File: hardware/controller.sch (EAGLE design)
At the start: 44 parts, among them J1 AVR_SPI_PRG_6NS, J10 22-27-2041-04, J11 22-27-2041-04, J2 ATX24RH, J3 22-27-2041-04, J4 22-27-2041-04, J5 22-27-2021-02, J6 22-27-2021-02, J7 22-27-2031-03, J8 22-27-2041-04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

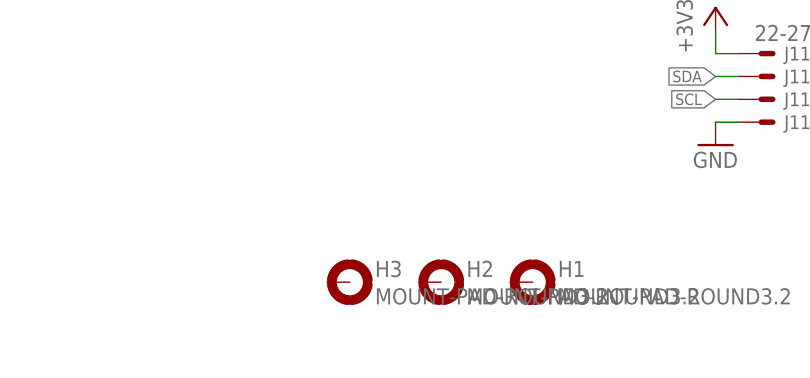
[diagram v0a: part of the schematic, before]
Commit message: Hardware: Add fourth hole and different crystal footprint.
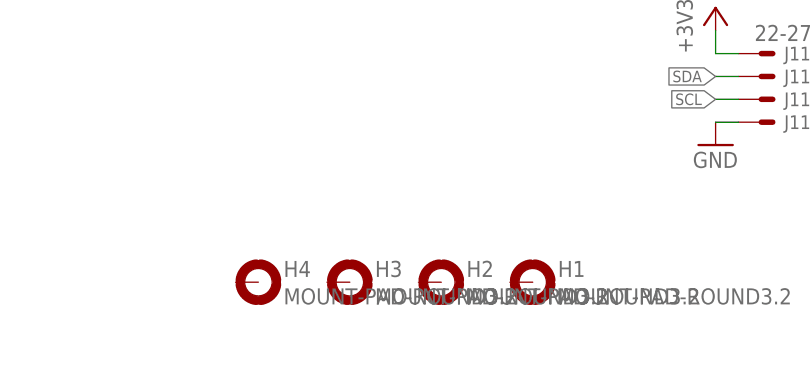
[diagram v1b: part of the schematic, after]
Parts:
- added H4: MOUNT-PAD-ROUND3.2, holes:MOUNT-PAD-ROUND3.2
- Y1: device SparkFun-FreqCtrl:CRYSTALSMD -> SparkFun-FreqCtrl:CRYSTALHC49UV
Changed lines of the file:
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@@
 <part name="P+1" library="supply1" deviceset="+5V" device=""/>
 <part name="J1" library="SparkFun-Connectors" deviceset="AVR_SPI_PRG_6" device="NS"/>
-<part name="Y1" library="SparkFun-FreqCtrl" deviceset="CRYSTAL" device="SMD"/>
+<part name="Y1" library="SparkFun-FreqCtrl" deviceset="CRYSTAL" device="HC49UV"/>
 <part name="P+2" library="supply1" deviceset="+5V" device=""/>
 <part name="GND2" library="supply1" deviceset="GND" device=""/>
@@
 <part name="R13" library="rcl" deviceset="R-EU_" device="R0603" value="1k"/>
 <part name="P+13" library="supply1" deviceset="+5V" device=""/>
+<part name="H4" library="holes" deviceset="MOUNT-PAD-ROUND" device="3.2"/>
 </parts>
 <sheets>
@@
 <instance part="R13" gate="G$1" x="20.32" y="81.28"/>
 <instance part="P+13" gate="1" x="12.7" y="86.36"/>
+<instance part="H4" gate="G$1" x="119.38" y="15.24"/>
 </instances>
 <busses>

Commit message: Hardware: Redesign layout of controller PCB.
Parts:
- removed R4: 1k, rcl:R-EU_R0603
- added C1, C2, C5, C6: (no value), rcl:C-EUC0603
- R1: value (none) -> 30
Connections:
- removed net N$8: R4.2, U$1.ALERT
- net +3V3: now also C5.1, C6.1, R13.1; no longer R4.1
- net +5V: now also C1.1, C2.1; no longer R13.1
- net GND: now also C1.2, C2.2, C5.2, C6.2
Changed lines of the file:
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@@
 <part name="+3V4" library="supply1" deviceset="+3V3" device=""/>
 <part name="+3V5" library="supply1" deviceset="+3V3" device=""/>
-<part name="R1" library="rcl" deviceset="R-EU_" device="R0603"/>
+<part name="R1" library="rcl" deviceset="R-EU_" device="R0603" value="30"/>
 <part name="R2" library="rcl" deviceset="R-EU_" device="R0603" value="56k"/>
 <part name="R3" library="rcl" deviceset="R-EU_" device="R0603" value="56k"/>
@@
 <part name="+3V6" library="supply1" deviceset="+3V3" device=""/>
 <part name="GND9" library="supply1" deviceset="GND" device=""/>
-<part name="R4" library="rcl" deviceset="R-EU_" device="R0603" value="1k"/>
 <part name="+3V8" library="supply1" deviceset="+3V3" device=""/>
 <part name="J2" library="hauser" deviceset="ATX24" device="RH"/>
@@
 <part name="H3" library="holes" deviceset="MOUNT-PAD-ROUND" device="3.2"/>
 <part name="R13" library="rcl" deviceset="R-EU_" device="R0603" value="1k"/>
-<part name="P+13" library="supply1" deviceset="+5V" device=""/>
 <part name="H4" library="holes" deviceset="MOUNT-PAD-ROUND" device="3.2"/>
+<part name="C1" library="rcl" deviceset="C-EU" device="C0603"/>
+<part name="C2" library="rcl" deviceset="C-EU" device="C0603"/>
+<part name="C5" library="rcl" deviceset="C-EU" device="C0603"/>
+<part name="C6" library="rcl" deviceset="C-EU" device="C0603"/>
+<part name="+3V10" library="supply1" deviceset="+3V3" device=""/>
+<part name="GND12" library="supply1" deviceset="GND" device=""/>
+<part name="P+14" library="supply1" deviceset="+5V" device=""/>
+<part name="+3V11" library="supply1" deviceset="+3V3" device=""/>
 </parts>
 <sheets>
@@
 <instance part="+3V6" gate="G$1" x="40.64" y="114.3"/>
 <instance part="GND9" gate="1" x="40.64" y="83.82"/>
-<instance part="R4" gate="G$1" x="63.5" y="99.06" rot="R270"/>
 <instance part="+3V8" gate="G$1" x="58.42" y="109.22"/>
 <instance part="J2" gate="G$1" x="228.6" y="147.32"/>
@@
 <instance part="H3" gate="G$1" x="129.54" y="15.24"/>
 <instance part="R13" gate="G$1" x="20.32" y="81.28"/>
-<instance part="P+13" gate="1" x="12.7" y="86.36"/>
 <instance part="H4" gate="G$1" x="119.38" y="15.24"/>
+<instance part="C1" gate="G$1" x="167.64" y="86.36"/>
+<instance part="C2" gate="G$1" x="175.26" y="86.36"/>
+<instance part="C5" gate="G$1" x="182.88" y="86.36"/>
+<instance part="C6" gate="G$1" x="190.5" y="86.36"/>
+<instance part="+3V10" gate="G$1" x="190.5" y="99.06"/>
+<instance part="GND12" gate="1" x="175.26" y="73.66"/>
+<instance part="P+14" gate="1" x="175.26" y="99.06"/>
+<instance part="+3V11" gate="G$1" x="12.7" y="86.36"/>
 </instances>
 <busses>
@@
 </segment>
 <segment>
-<pinref part="R13" gate="G$1" pin="1"/>
-<pinref part="P+13" gate="1" pin="+5V"/>
-<wire x1="15.24" y1="81.28" x2="12.7" y2="81.28" width="0.1524" layer="91"/>
-<wire x1="12.7" y1="81.28" x2="12.7" y2="83.82" width="0.1524" layer="91"/>
+<pinref part="C2" gate="G$1" pin="1"/>
+<pinref part="P+14" gate="1" pin="+5V"/>
+<wire x1="175.26" y1="88.9" x2="175.26" y2="91.44" width="0.1524" layer="91"/>
+<pinref part="C1" gate="G$1" pin="1"/>
+<wire x1="175.26" y1="91.44" x2="175.26" y2="96.52" width="0.1524" layer="91"/>
+<wire x1="167.64" y1="88.9" x2="167.64" y2="91.44" width="0.1524" layer="91"/>
+<wire x1="167.64" y1="91.44" x2="175.26" y2="91.44" width="0.1524" layer="91"/>
+<junction x="175.26" y="91.44"/>
 </segment>
 </net>
@@
 <junction x="111.76" y="116.84"/>
 </segment>
+<segment>
+<pinref part="C1" gate="G$1" pin="2"/>
+<wire x1="167.64" y1="81.28" x2="167.64" y2="78.74" width="0.1524" layer="91"/>
+<wire x1="167.64" y1="78.74" x2="175.26" y2="78.74" width="0.1524" layer="91"/>
+<pinref part="C2" gate="G$1" pin="2"/>
+<wire x1="175.26" y1="78.74" x2="175.26" y2="81.28" width="0.1524" layer="91"/>
+<pinref part="GND12" gate="1" pin="GND"/>
+<wire x1="175.26" y1="76.2" x2="175.26" y2="78.74" width="0.1524" layer="91"/>
+<junction x="175.26" y="78.74"/>
+<pinref part="C6" gate="G$1" pin="2"/>
+<wire x1="190.5" y1="81.28" x2="190.5" y2="78.74" width="0.1524" layer="91"/>
+<wire x1="190.5" y1="78.74" x2="182.88" y2="78.74" width="0.1524" layer="91"/>
+<pinref part="C5" gate="G$1" pin="2"/>
+<wire x1="182.88" y1="78.74" x2="175.26" y2="78.74" width="0.1524" layer="91"/>
+<wire x1="182.88" y1="81.28" x2="182.88" y2="78.74" width="0.1524" layer="91"/>
+<junction x="182.88" y="78.74"/>
+</segment>
 </net>
 <net name="N$1" class="0">
@@
 <wire x1="55.88" y1="99.06" x2="58.42" y2="99.06" width="0.1524" layer="91"/>
 <pinref part="+3V8" gate="G$1" pin="+3V3"/>
-<pinref part="R4" gate="G$1" pin="1"/>
-<wire x1="63.5" y1="104.14" x2="58.42" y2="104.14" width="0.1524" layer="91"/>
 </segment>
 <segment>
@@
 <junction x="243.84" y="165.1"/>
 </segment>
+<segment>
+<pinref part="C6" gate="G$1" pin="1"/>
+<pinref part="+3V10" gate="G$1" pin="+3V3"/>
+<wire x1="190.5" y1="88.9" x2="190.5" y2="91.44" width="0.1524" layer="91"/>
+<pinref part="C5" gate="G$1" pin="1"/>
+<wire x1="190.5" y1="91.44" x2="190.5" y2="96.52" width="0.1524" layer="91"/>
+<wire x1="182.88" y1="88.9" x2="182.88" y2="91.44" width="0.1524" layer="91"/>
+<wire x1="182.88" y1="91.44" x2="190.5" y2="91.44" width="0.1524" layer="91"/>
+<junction x="190.5" y="91.44"/>
+</segment>
+<segment>
+<pinref part="R13" gate="G$1" pin="1"/>
+<wire x1="15.24" y1="81.28" x2="12.7" y2="81.28" width="0.1524" layer="91"/>
+<wire x1="12.7" y1="81.28" x2="12.7" y2="83.82" width="0.1524" layer="91"/>
+<pinref part="+3V11" gate="G$1" pin="+3V3"/>
+</segment>
 </net>
 <net name="N$3" class="0">
@@
 </segment>
 </net>
-<net name="N$8" class="0">
-<segment>
-<pinref part="U$1" gate="G$1" pin="ALERT"/>
-<pinref part="R4" gate="G$1" pin="2"/>
-<wire x1="55.88" y1="93.98" x2="63.5" y2="93.98" width="0.1524" layer="91"/>
-</segment>
-</net>

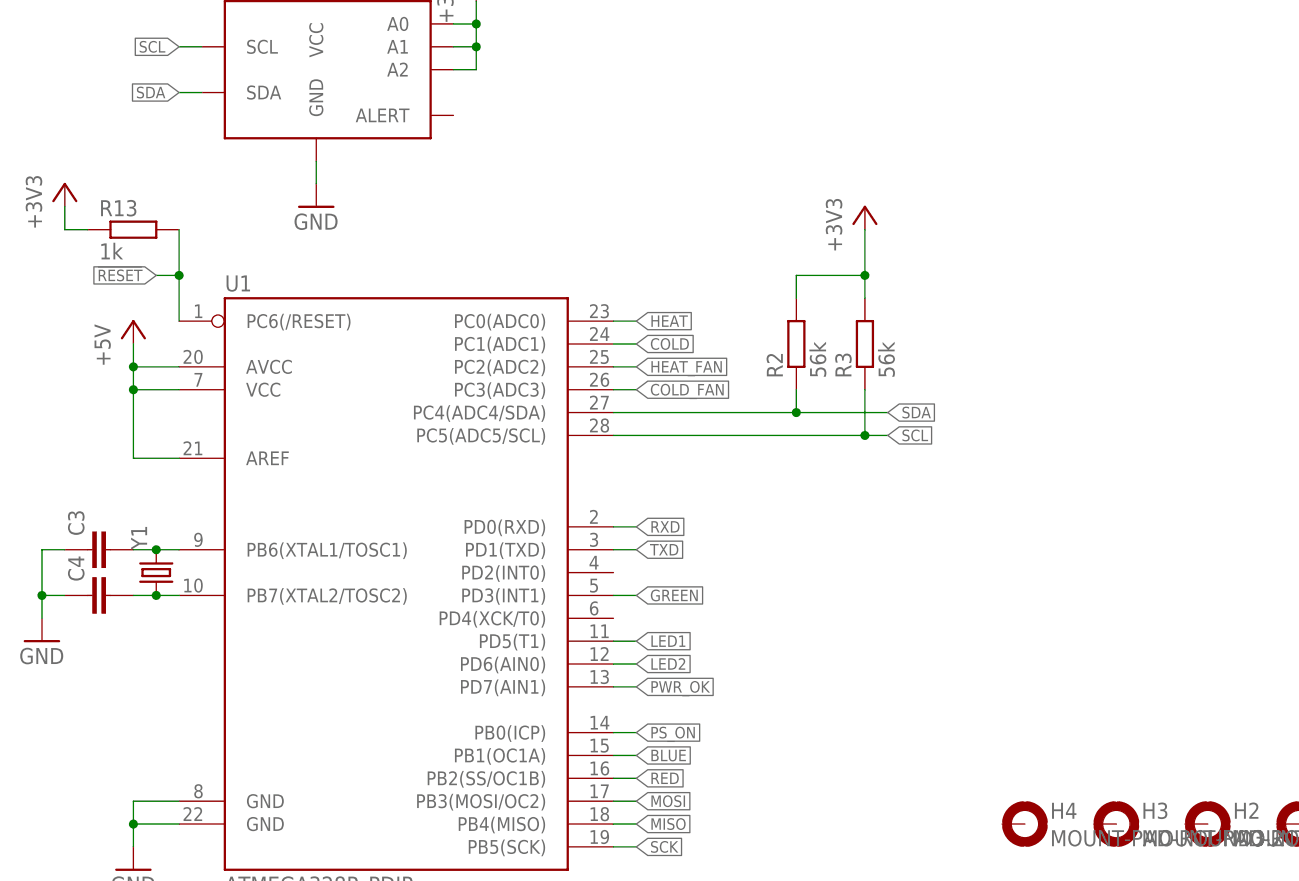
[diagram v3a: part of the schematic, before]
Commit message: Hardware: Add reset push button to PCB.
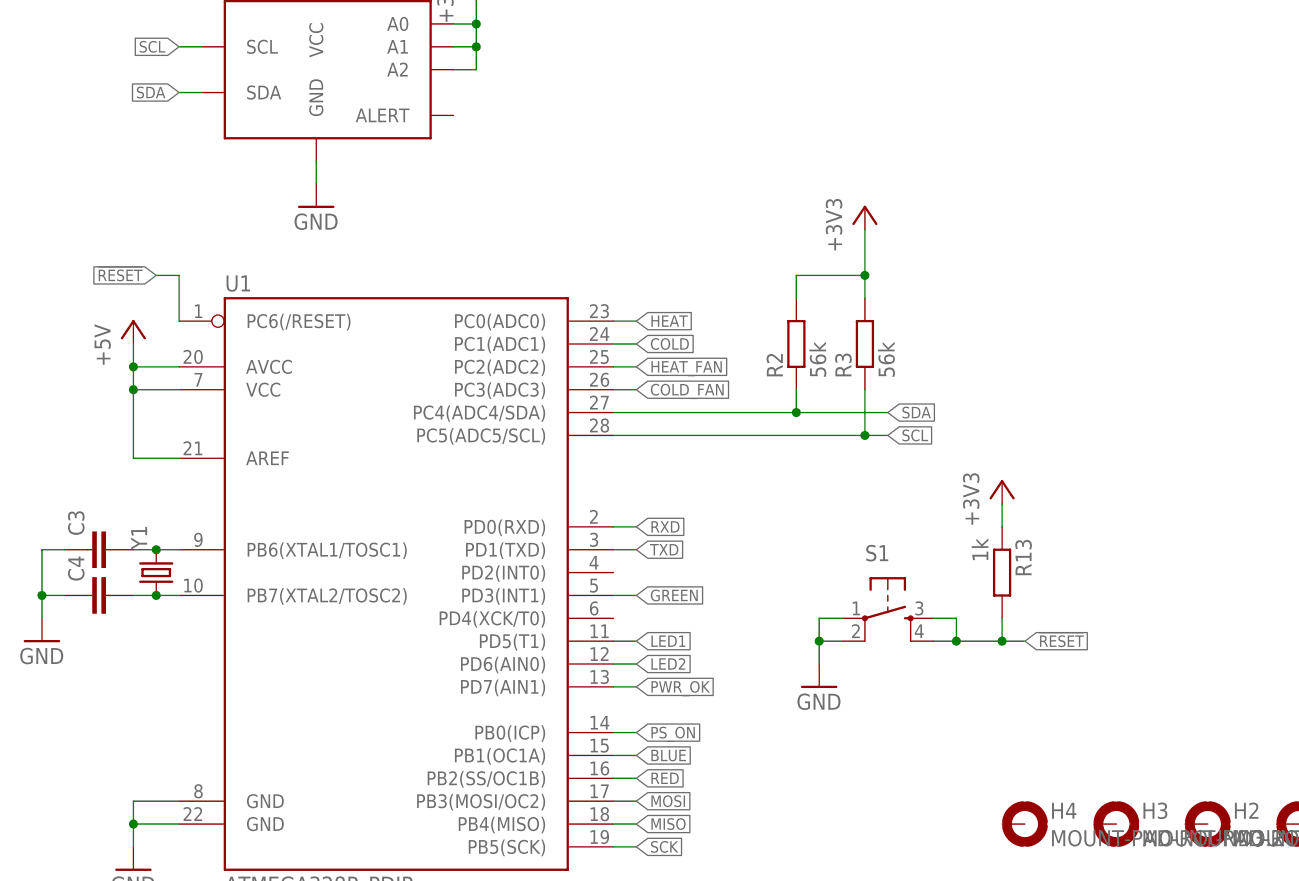
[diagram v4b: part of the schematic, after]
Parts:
- added S1: (no value), SparkFun-Electromechanical:TAC_SWITCHPTH
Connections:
- net !RESET: now also S1.3, S1.4
- net GND: now also S1.1, S1.2
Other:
- moved on the sheet: R13
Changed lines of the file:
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@@
 <part name="P+14" library="supply1" deviceset="+5V" device=""/>
 <part name="+3V11" library="supply1" deviceset="+3V3" device=""/>
+<part name="S1" library="SparkFun-Electromechanical" deviceset="TAC_SWITCH" device="PTH"/>
+<part name="GND13" library="supply1" deviceset="GND" device=""/>
 </parts>
 <sheets>
@@
 <instance part="H2" gate="G$1" x="139.7" y="15.24"/>
 <instance part="H3" gate="G$1" x="129.54" y="15.24"/>
-<instance part="R13" gate="G$1" x="20.32" y="81.28"/>
+<instance part="R13" gate="G$1" x="116.84" y="43.18" rot="R270"/>
 <instance part="H4" gate="G$1" x="119.38" y="15.24"/>
 <instance part="C1" gate="G$1" x="167.64" y="86.36"/>
@@
 <instance part="GND12" gate="1" x="175.26" y="73.66"/>
 <instance part="P+14" gate="1" x="175.26" y="99.06"/>
-<instance part="+3V11" gate="G$1" x="12.7" y="86.36"/>
+<instance part="+3V11" gate="G$1" x="116.84" y="53.34"/>
+<instance part="S1" gate="S" x="104.14" y="38.1"/>
+<instance part="GND13" gate="1" x="96.52" y="30.48"/>
 </instances>
 <busses>
@@
 <junction x="182.88" y="78.74"/>
 </segment>
+<segment>
+<pinref part="S1" gate="S" pin="1"/>
+<wire x1="99.06" y1="38.1" x2="96.52" y2="38.1" width="0.1524" layer="91"/>
+<wire x1="96.52" y1="38.1" x2="96.52" y2="35.56" width="0.1524" layer="91"/>
+<pinref part="S1" gate="S" pin="2"/>
+<wire x1="96.52" y1="35.56" x2="96.52" y2="33.02" width="0.1524" layer="91"/>
+<wire x1="99.06" y1="35.56" x2="96.52" y2="35.56" width="0.1524" layer="91"/>
+<junction x="96.52" y="35.56"/>
+<pinref part="GND13" gate="1" pin="GND"/>
+</segment>
 </net>
 <net name="N$1" class="0">
@@
 <net name="!RESET" class="0">
 <segment>
-<pinref part="U1" gate="G$1" pin="PC6(/RESET)"/>
-<wire x1="25.4" y1="71.12" x2="25.4" y2="76.2" width="0.1524" layer="91"/>
-<wire x1="25.4" y1="76.2" x2="22.86" y2="76.2" width="0.1524" layer="91"/>
-<label x="22.86" y="76.2" size="1.27" layer="95" rot="R180" xref="yes"/>
 <pinref part="R13" gate="G$1" pin="2"/>
-<wire x1="25.4" y1="76.2" x2="25.4" y2="81.28" width="0.1524" layer="91"/>
-<junction x="25.4" y="76.2"/>
+<pinref part="S1" gate="S" pin="4"/>
+<wire x1="109.22" y1="35.56" x2="111.76" y2="35.56" width="0.1524" layer="91"/>
+<pinref part="S1" gate="S" pin="3"/>
+<wire x1="111.76" y1="35.56" x2="116.84" y2="35.56" width="0.1524" layer="91"/>
+<wire x1="116.84" y1="35.56" x2="116.84" y2="38.1" width="0.1524" layer="91"/>
+<wire x1="109.22" y1="38.1" x2="111.76" y2="38.1" width="0.1524" layer="91"/>
+<wire x1="111.76" y1="38.1" x2="111.76" y2="35.56" width="0.1524" layer="91"/>
+<junction x="111.76" y="35.56"/>
+<wire x1="116.84" y1="35.56" x2="119.38" y2="35.56" width="0.1524" layer="91"/>
+<junction x="116.84" y="35.56"/>
+<label x="119.38" y="35.56" size="1.27" layer="95" xref="yes"/>
 </segment>
 <segment>
@@
 <wire x1="218.44" y1="93.98" x2="215.9" y2="93.98" width="0.1524" layer="91"/>
 <label x="215.9" y="93.98" size="1.27" layer="95" rot="R180" xref="yes"/>
+</segment>
+<segment>
+<wire x1="25.4" y1="76.2" x2="22.86" y2="76.2" width="0.1524" layer="91"/>
+<pinref part="U1" gate="G$1" pin="PC6(/RESET)"/>
+<wire x1="25.4" y1="71.12" x2="25.4" y2="76.2" width="0.1524" layer="91"/>
+<label x="22.86" y="76.2" size="1.27" layer="95" rot="R180" xref="yes"/>
 </segment>
 </net>
@@
 <segment>
 <pinref part="R13" gate="G$1" pin="1"/>
-<wire x1="15.24" y1="81.28" x2="12.7" y2="81.28" width="0.1524" layer="91"/>
-<wire x1="12.7" y1="81.28" x2="12.7" y2="83.82" width="0.1524" layer="91"/>
+<wire x1="116.84" y1="48.26" x2="116.84" y2="50.8" width="0.1524" layer="91"/>
 <pinref part="+3V11" gate="G$1" pin="+3V3"/>
 </segment>
